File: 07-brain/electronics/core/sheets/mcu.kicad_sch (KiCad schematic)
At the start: 1 part, among them U3 Pico

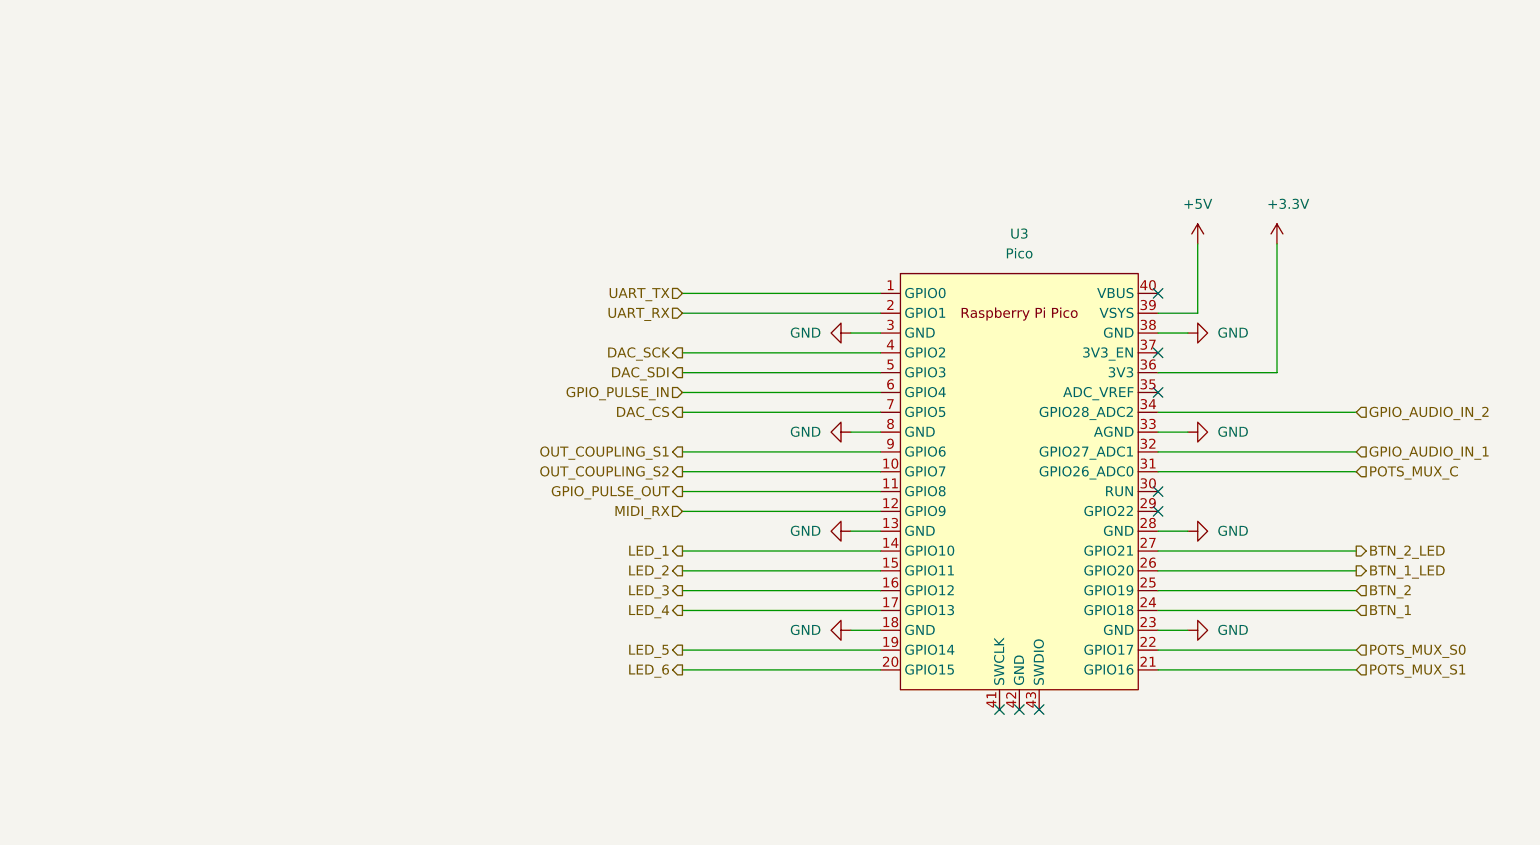
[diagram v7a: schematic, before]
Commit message: Updated USB-C breakout on Brain Core
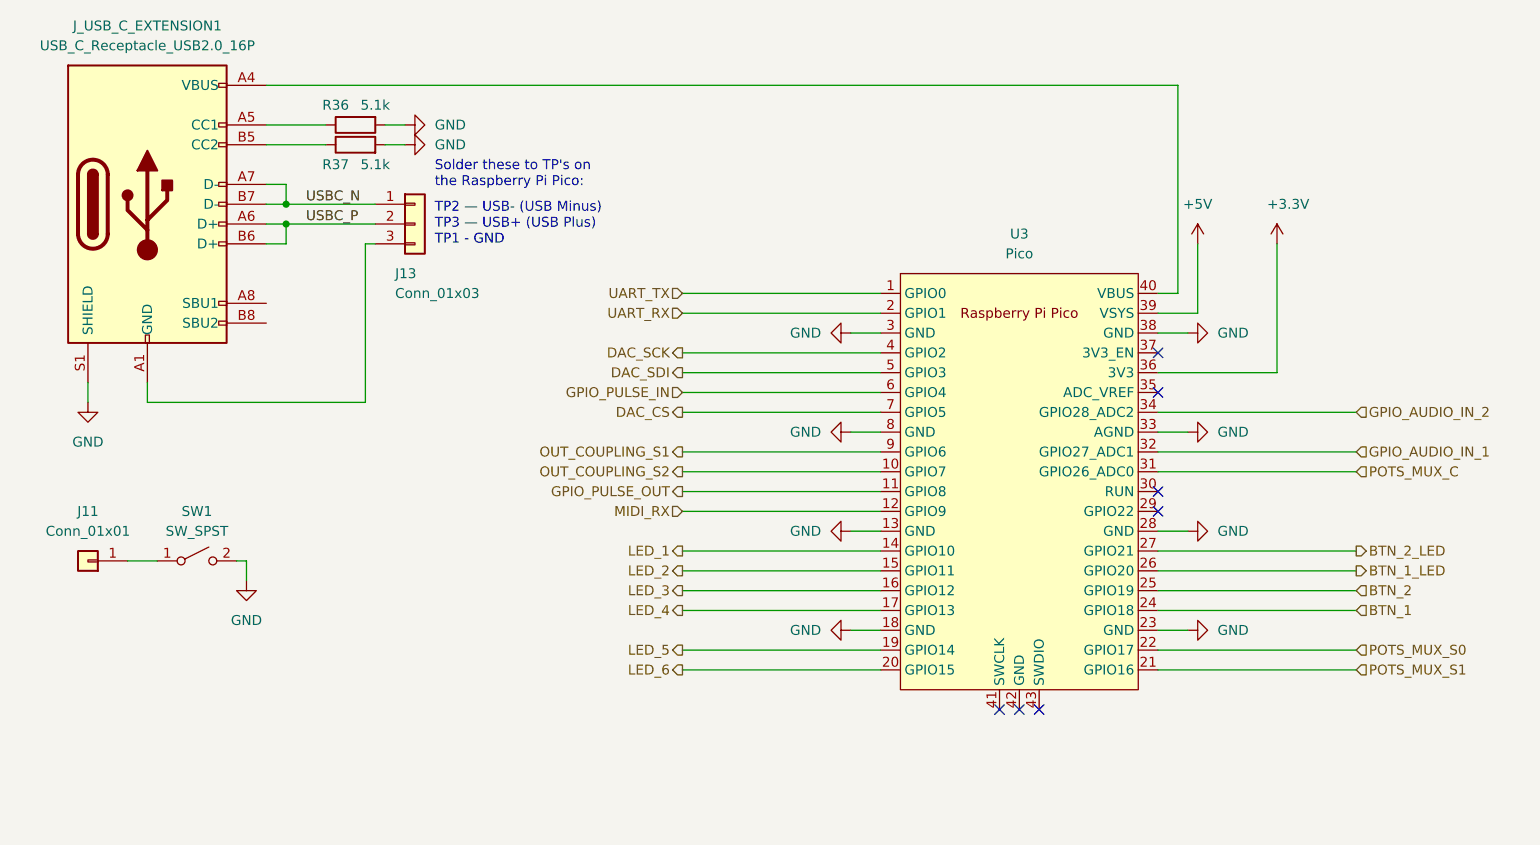
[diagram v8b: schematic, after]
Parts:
- added J11: Conn_01x01, Connector_PinHeader_2.54mm:PinHeader_1x01_P2.54mm_Vertical, symbol Connector_Generic:Conn_01x01
- added J13: Conn_01x03, Connector_PinHeader_2.54mm:PinHeader_1x03_P2.54mm_Vertical, symbol Connector_Generic:Conn_01x03
- added J_USB_C_EXTENSION1: USB_C_Receptacle_USB2.0_16P, Connector_USB:USB_C_Receptacle_HRO_TYPE-C-31-M-12, symbol Connector:USB_C_Receptacle_USB2.0_16P
- added R36, R37: 5.1k, Resistor_SMD:R_0603_1608Metric, symbol Device:R
- added SW1: SW_SPST, Button_Switch_THT:SW_Tactile_SKHH_Angled, symbol Switch:SW_SPST
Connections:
- net GND: now also J_USB_C_EXTENSION1.S1 (SHIELD), R36.2, R37.2, SW1.2 (B)
- net at U3.40 (VBUS): now also J_USB_C_EXTENSION1.A4 (VBUS), J_USB_C_EXTENSION1.A9 (VBUS), J_USB_C_EXTENSION1.B4 (VBUS), J_USB_C_EXTENSION1.B9 (VBUS)
- new net: J11.1 (Pin_1), SW1.1 (A)
- new net: J13.3 (Pin_3), J_USB_C_EXTENSION1.A1 (GND), J_USB_C_EXTENSION1.A12 (GND), J_USB_C_EXTENSION1.B1 (GND), J_USB_C_EXTENSION1.B12 (GND)
- new net: J_USB_C_EXTENSION1.A5 (CC1), R36.1
- new net: J_USB_C_EXTENSION1.B5 (CC2), R37.1
- new net USBC_N: J13.1 (Pin_1), J_USB_C_EXTENSION1.A7 (D-), J_USB_C_EXTENSION1.B7 (D-)
- new net USBC_P: J13.2 (Pin_2), J_USB_C_EXTENSION1.A6 (D+), J_USB_C_EXTENSION1.B6 (D+)
- no-connect marks 8 -> 7
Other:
- note added: "Solder these to TP's on the Raspberry Pi Pico:"
- note added: "TP2 — USB- (USB Minus) TP3 — USB+ (USB Plus) TP1 - GND"
